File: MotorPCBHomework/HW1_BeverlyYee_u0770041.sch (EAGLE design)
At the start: 20 parts, among them J1 CON-SOCJ-2155, U1 L298N, U2 LM75AIMX

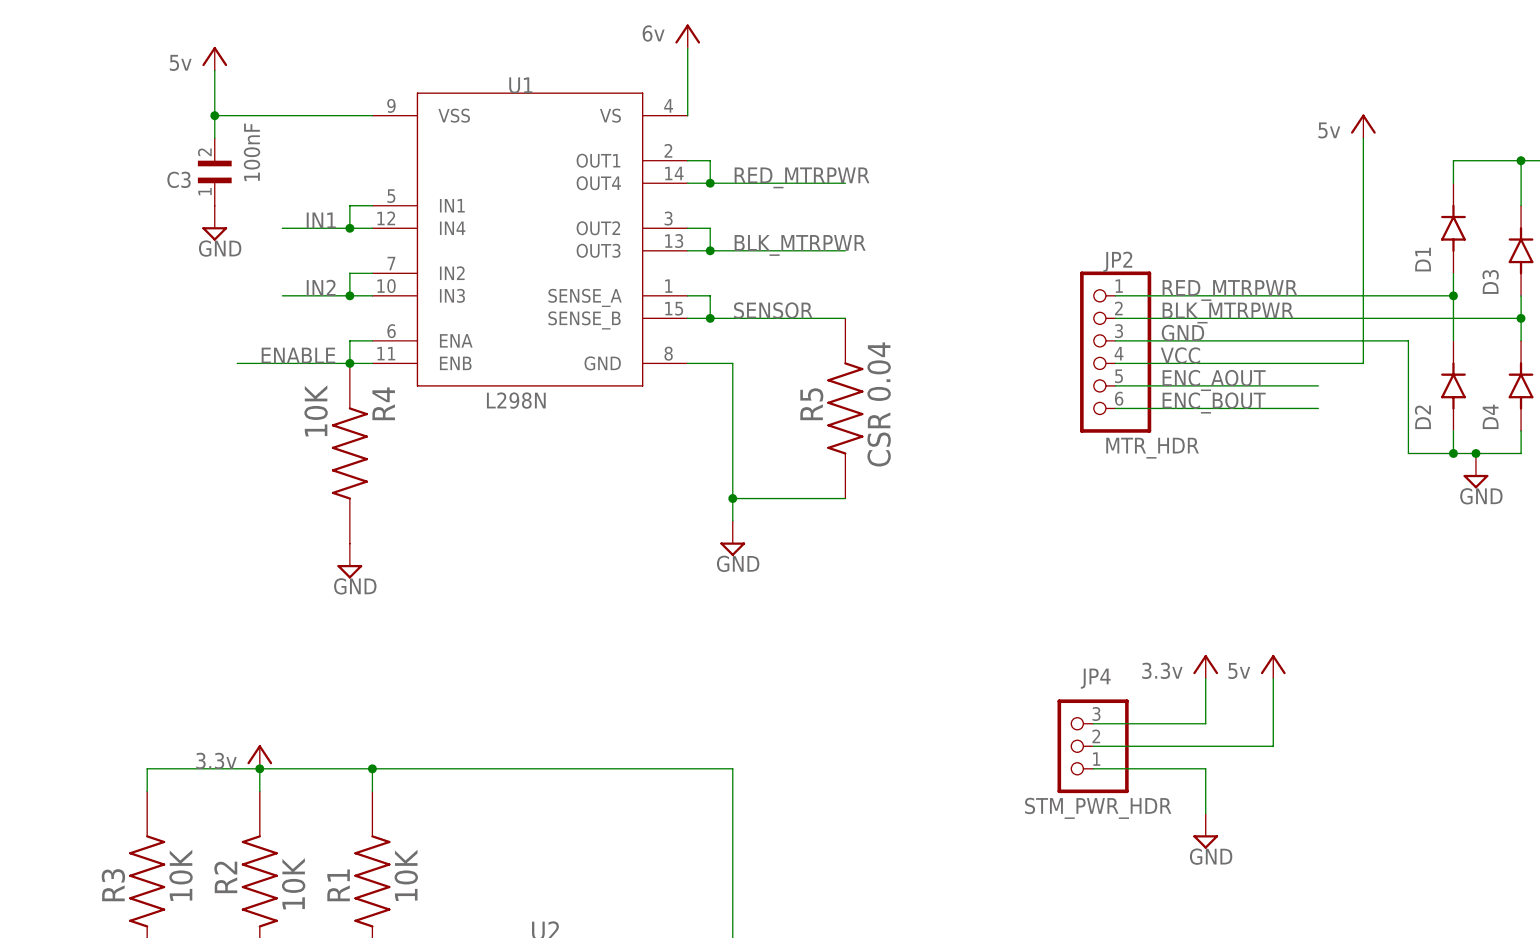
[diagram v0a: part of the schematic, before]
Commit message: Eliminate all airwires
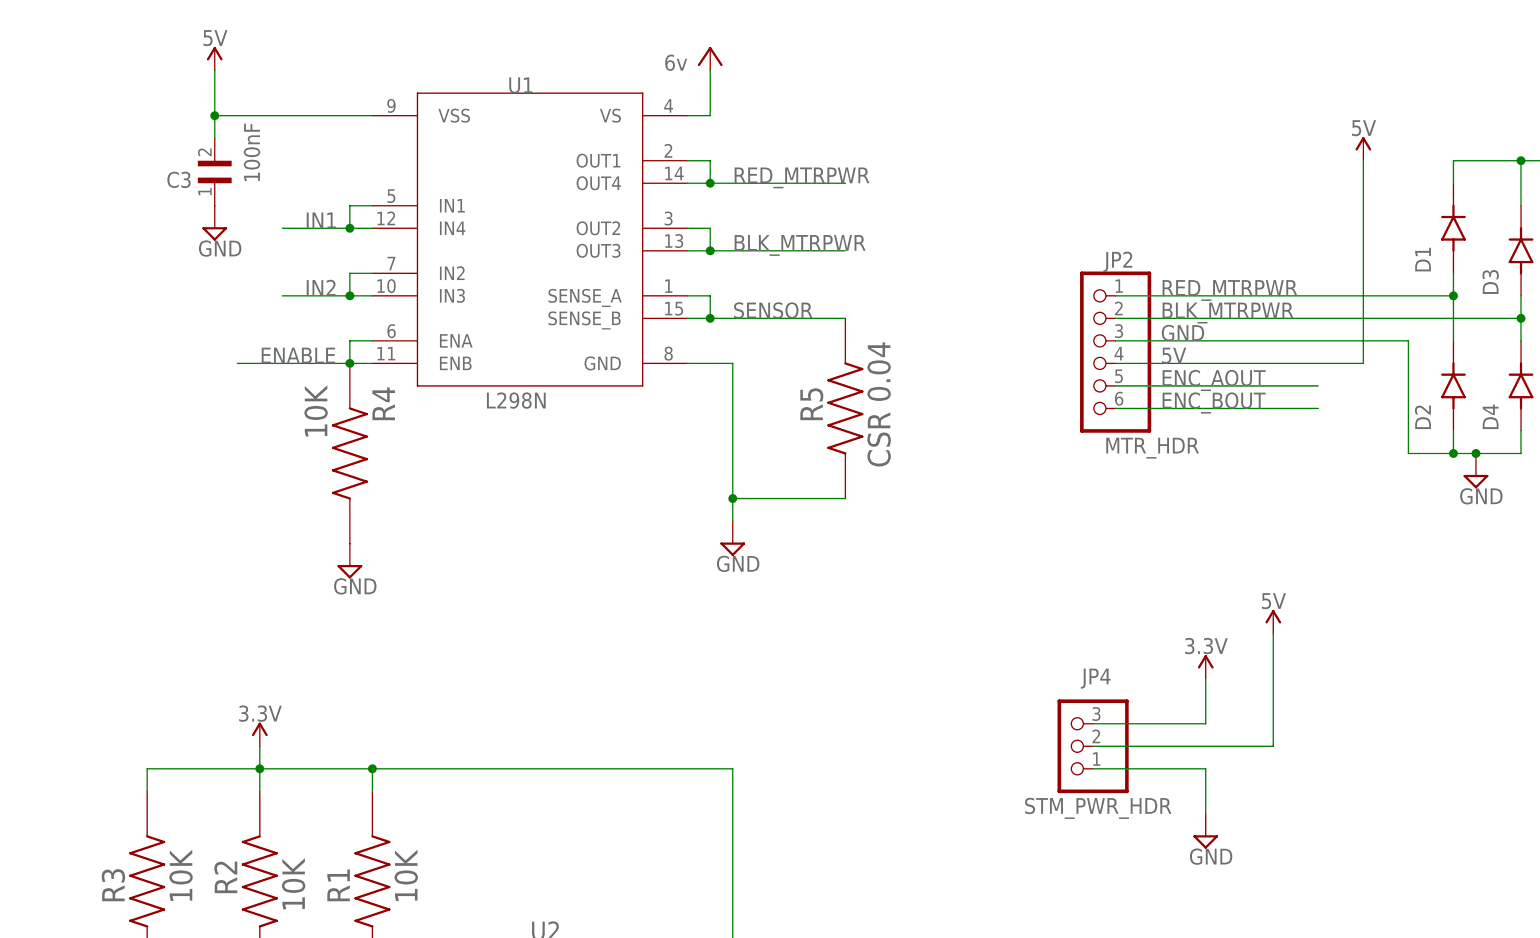
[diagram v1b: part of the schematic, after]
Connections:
- new net 3.3V: C4.1, JP4.3, R1.2, R2.1, R3.2, U2.VS+
- new net 5V: C3.2, JP2.4, JP4.2, U1.VSS
- net VCC: no longer C3.2, C4.1, JP2.4, JP4.2, JP4.3, R1.2, R2.1, R3.2, U1.VSS, U2.VS+
